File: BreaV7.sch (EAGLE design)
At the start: 32 parts, among them J2 XF2L-0535-1, J3 XF2L-0635-1, Q1 ABM-16MHZ, SW1 LS12T2-T, SW2 EVQ11U09K, SW3 ESE31L11T, U2 TPS62200, X1 22-23-2021

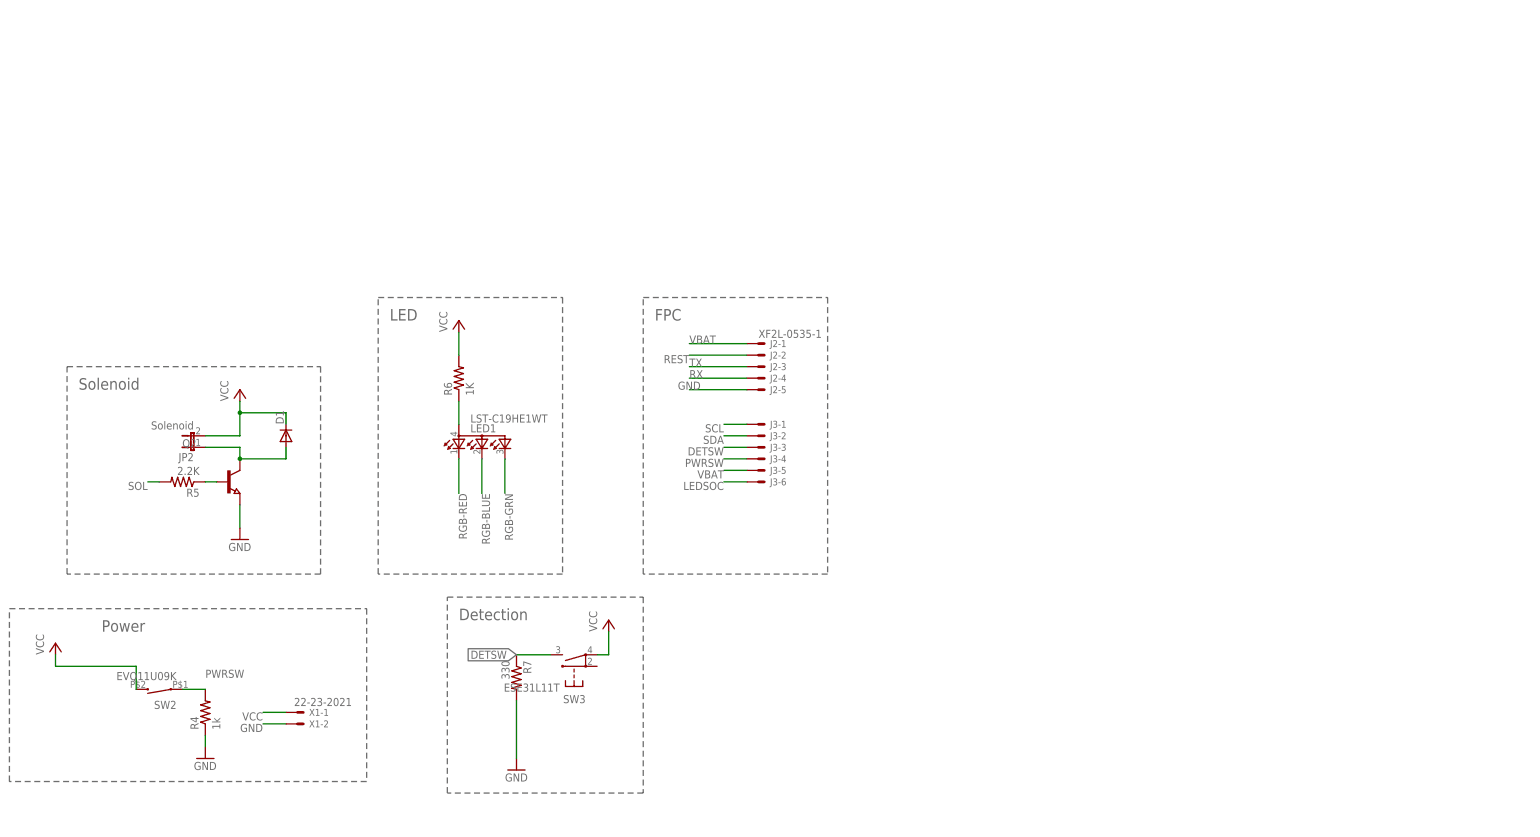
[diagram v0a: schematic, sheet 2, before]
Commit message: Combined boards
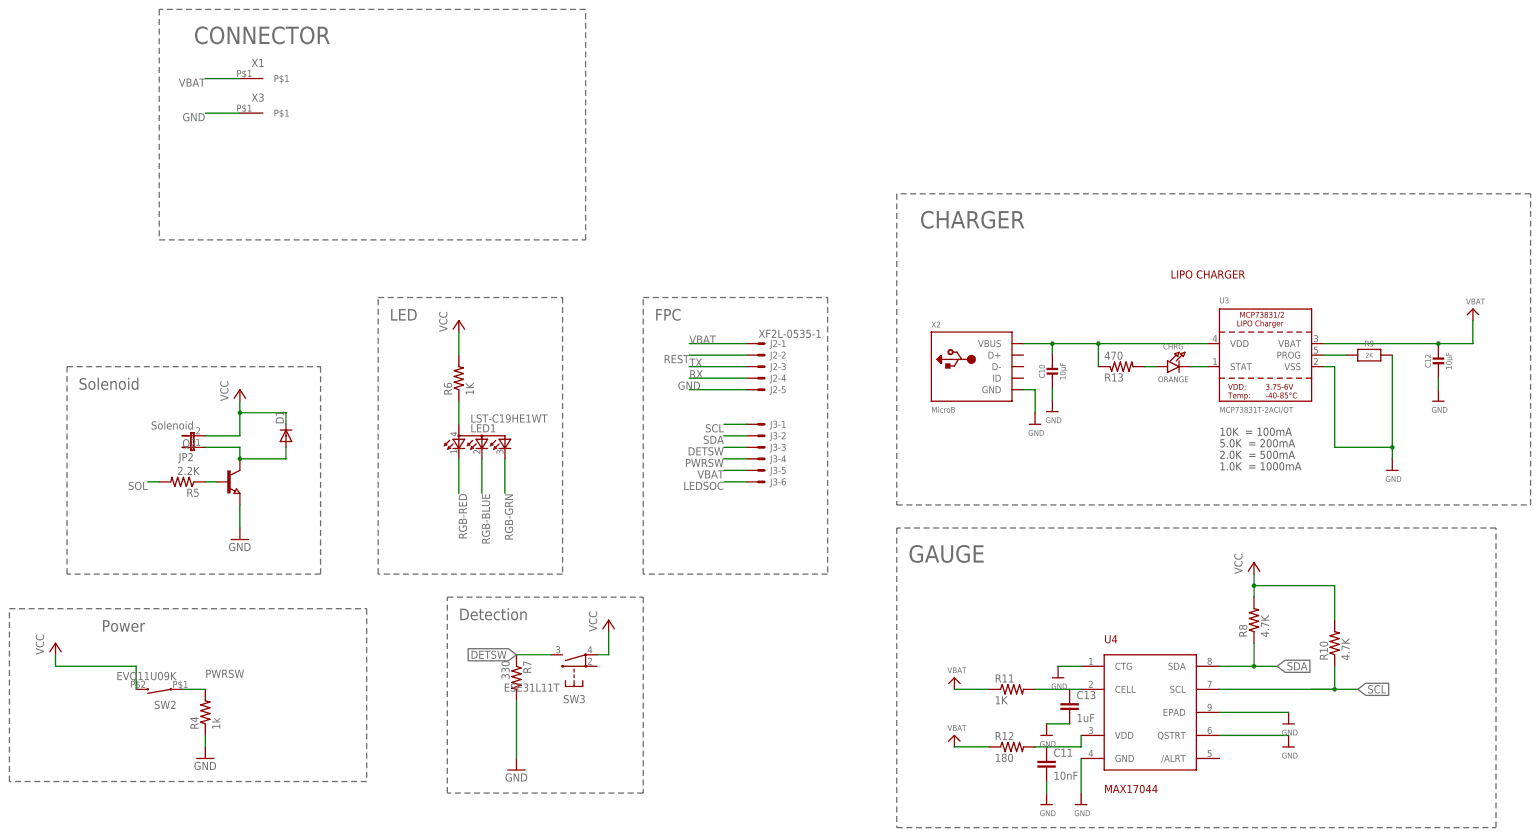
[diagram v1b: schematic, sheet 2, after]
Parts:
- added C10, C12: 10µF, microbuilder:CAP_CERAMIC0805-NOOUTLINE
- added C11: 10nF, rcl:C-EUC0603
- added C13: 1uF, rcl:C-EUC0603
- added CHRG: ORANGE, microbuilder:LED0805_NOOUTLINE
- added R10, R8: 4.7K, resistor:R-US_R0402
- added R11: 1K, resistor:R-US_R0402
- added R12: 180, resistor:R-US_R0402
- added R13: 470, resistor:R-US_R0402
- added R9: 2K, microbuilder:RESISTOR0805_NOOUTLINE
- added U3: MCP73831T-2ACI/OT, microbuilder:MCP73831/2
- added U4: MAX17044, NewPart:MAX17044
- added X2: MicroB, microbuilder:USBMICRO_20329
- added X3: CON-1PIN, NewPart:CON-1PIN
- X1: value 22-23-2021 -> CON-1PIN; device con-molex:22-23-2021 -> NewPart:CON-1PIN
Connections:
- new net N$11: CHRG.C, U3.STAT
- new net N$14: R9.1, U3.PROG
- new net N$4: C13.1, R11.2, U4.CELL
- new net N$6: C11.1, R12.2, U4.VDD
- new net N$8: CHRG.A, R13.2
- new net VBUS1: C10.1, R13.1, U3.VDD, X2.VBUS
- net GND: now also C10.2, C11.2, C12.2, C13.2, R9.2, U3.VSS, U4.CTG, U4.EPAD, U4.GND, U4.QSTRT, X2.GND, X3.P$1; no longer X1-2.S
- net SCL: now also R10.1, U4.SCL
- net SDA: now also R8.1, U4.SDA
- net VBAT: now also C12.1, R10.2, R11.1, R12.1, R8.2, U3.VBAT, X1.P$1
- net VCC: no longer X1-1.S
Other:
- note added: "1.0K = 1000mA"
- note added: "10K = 100mA"
- note added: "2.0K = 500mA"
- note added: "5.0K = 200mA"
- note added: "CHARGER"
- note added: "CONNECTOR"
- note added: "GAUGE"
- note added: "LIPO CHARGER"

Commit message: 4-layer board
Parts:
- removed C10, C12: 10µF, microbuilder:CAP_CERAMIC0805-NOOUTLINE
- removed C11: 10nF, rcl:C-EUC0603
- removed C13: 1uF, rcl:C-EUC0603
- removed CHRG: ORANGE, microbuilder:LED0805_NOOUTLINE
- removed J3: XF2L-0635-1, con-omron:XF2L-0635-1
- removed R10: 4.7K, resistor:R-US_R0402
- removed R11: 1K, resistor:R-US_R0402
- removed R12: 180, resistor:R-US_R0402
- removed R13: 470, resistor:R-US_R0402
- removed R9: 2K, microbuilder:RESISTOR0805_NOOUTLINE
- removed U3: MCP73831T-2ACI/OT, microbuilder:MCP73831/2
- removed U4: MAX17044, NewPart:MAX17044
- removed X2: MicroB, microbuilder:USBMICRO_20329
- added C14, C16: 10µF, microbuilder:CAP_CERAMIC0805-NOOUTLINE
- added C15: 10nF, rcl:C-EUC0603
- added C17: 1uF, rcl:C-EUC0603
- added CHRG1: ORANGE, microbuilder:LED0805_NOOUTLINE
- added R15, R16: 4.7K, resistor:R-US_R0402
- added R17: 1K, resistor:R-US_R0402
- added R18: 180, resistor:R-US_R0402
- added R19: 470, resistor:R-US_R0402
- added U5: MCP73831T-2ACI/OT, microbuilder:MCP73831/2
- added U6: MAX17044, NewPart:MAX17044
- added X4: MicroB, microbuilder:USBMICRO_20329
- R8: value 4.7K -> 2K
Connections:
- removed net N$11: CHRG.C, U3.STAT
- removed net N$14: R9.1, U3.PROG
- removed net N$4: C13.1, R11.2, U4.CELL
- removed net N$6: C11.1, R12.2, U4.VDD
- removed net N$8: CHRG.A, R13.2
- removed net VBAT: C12.1, J2-1.MSV, J3-5.MS, R10.2, R11.1, R12.1, R8.2, U3.VBAT, X1.P$1
- removed net VBUS1: C10.1, R13.1, U3.VDD, X2.VBUS
- new net N$12: R8.1, U5.PROG
- new net N$13: C17.1, R17.2, U6.CELL
- new net N$15: C15.1, R18.2, U6.VDD
- new net N$16: CHRG1.A, R19.2
- new net N$17: CHRG1.C, U5.STAT
- new net VBUS2: C14.1, R19.1, U5.VDD, X4.VBUS
- net DETSW: no longer J3-3.MS
- net GND: now also C14.2, C15.2, C16.2, C17.2, R8.2, U5.VSS, U6.CTG, U6.EPAD, U6.GND, U6.QSTRT, X4.GND; no longer C10.2, C11.2, C12.2, C13.2, R9.2, U3.VSS, U4.CTG, U4.EPAD, U4.GND, U4.QSTRT, X2.GND
- net LEDSOC: no longer J3-6.MS
- net PWRSW: no longer J3-4.MS
- net SCL: now also R16.1, U6.SCL; no longer J3-1.MS, R10.1, U4.SCL
- net SDA: now also R15.1, U6.SDA; no longer J3-2.MS, R8.1, U4.SDA
- net VCC: now also C16.1, J2-1.MSV, R15.2, R16.2, R17.1, R18.1, U5.VBAT, X1.P$1
